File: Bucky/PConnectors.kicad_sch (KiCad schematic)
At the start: 52 parts, among them IC4 LTC4372CMS8#TRPBF, IC5 LTC4372CMS8#TRPBF, IC701 LTC4372CMS8#TRPBF, IC702 LTC4372CMS8#TRPBF, J1 XT60PW-M, J11 XT30AW-M, J12 XT30AW-M, J13 XT30AW-M, J14 XT30AW-M, J17 XT30UPB-F, J18 XT30UPB-F, J2 XT60PW-F, J3 XT30PW-F, J4 XT30PW-F, J5 XT30PW-F, J6 XT30PW-F, J7 XT30UPB-F, J8 XT30UPB-F, Q1 ISC016N04NM7V, Q2 ISC016N04NM7V, Q3 ISC016N04NM7V, Q4 ISC016N04NM7V, Q5 ISC016N04NM7V, Q6 ISC016N04NM7V, Q7 ISC016N04NM7V, Q8 ISC016N04NM7V

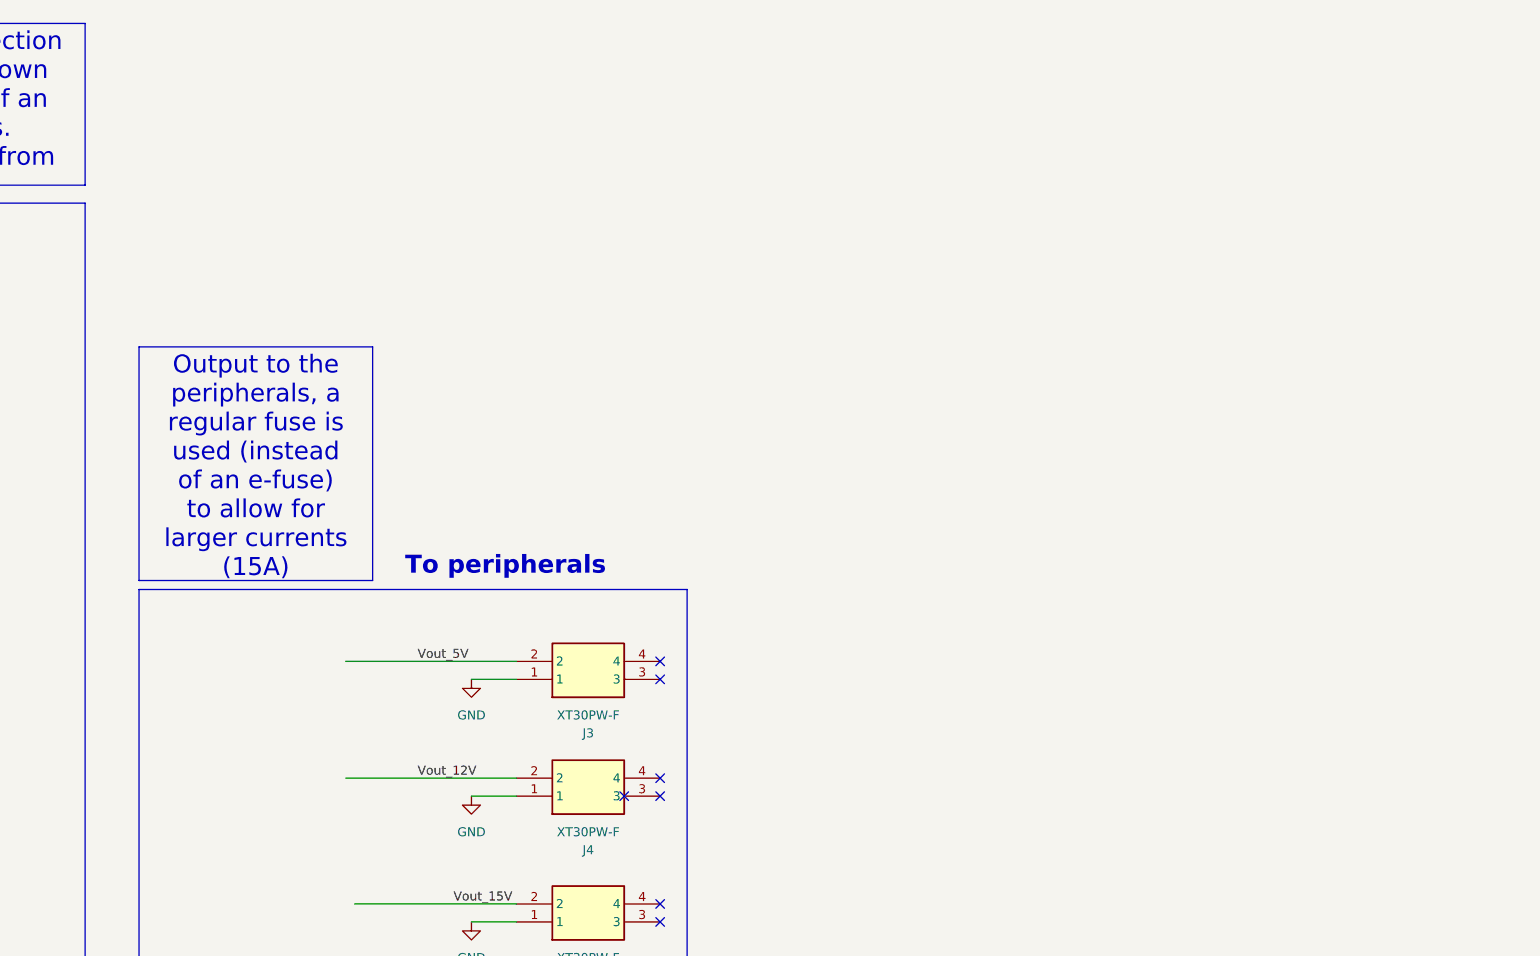
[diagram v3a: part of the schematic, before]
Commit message: created Bucky++ with new template and e-fuses
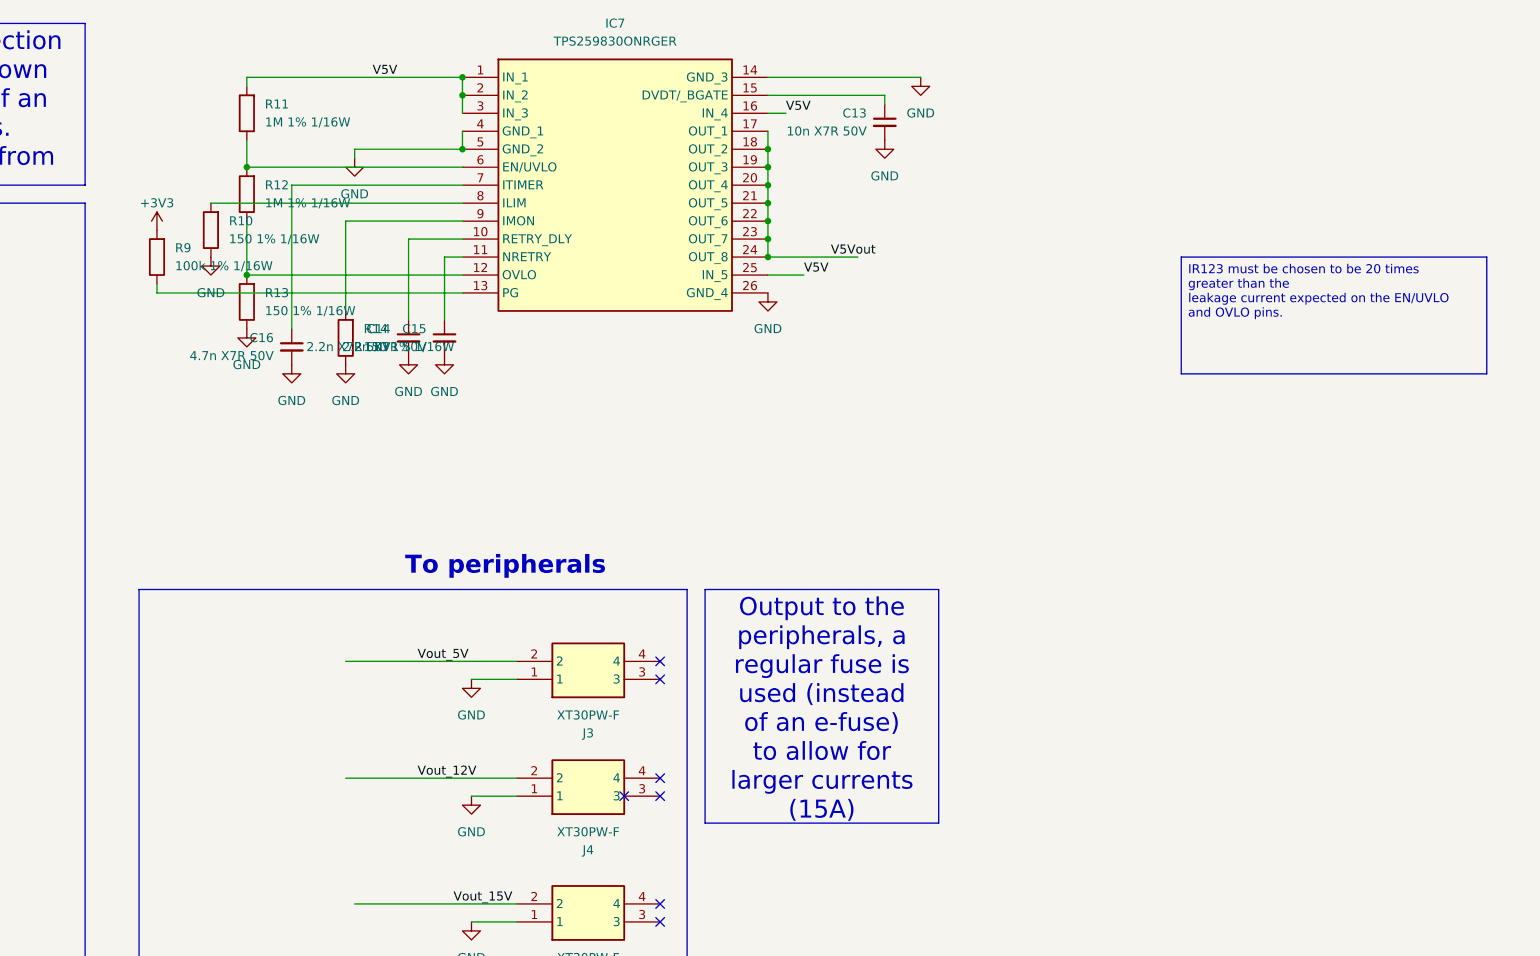
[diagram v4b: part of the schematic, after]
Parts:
- added C13: 10n X7R 50V, 0_capacitor_smd:C_0402_1005_DensityHigh, symbol Device:C_Small
- added C14, C15: 2.2n X7R 50V, 0_capacitor_smd:C_0402_1005_DensityHigh, symbol Device:C_Small
- added C16: 4.7n X7R 50V, 0_capacitor_smd:C_0402_1005_DensityHigh, symbol Device:C_Small
- added IC7: TPS259830ONRGER, TPS259830ONRGER, symbol SamacSys_Parts:TPS259830ONRGER
- added R10, R13, R14: 150 1% 1/16W, 0_resistor_smd:R_0402_1005_DensityHigh, symbol Device:R
- added R11, R12: 1M 1% 1/16W, 0_resistor_smd:R_0402_1005_DensityHigh, symbol Device:R
- added R9: 100k 1% 1/16W, 0_resistor_smd:R_0402_1005_DensityHigh, symbol Device:R
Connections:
- net GND: now also C13.2, C14.2, C15.2, C16.2, IC7.14 (GND_3), IC7.26 (GND_4), IC7.4 (GND_1), IC7.5 (GND_2), R10.1, R13.1, R14.1
- new net: C14.1, IC7.10 (RETRY_DLY)
- new net: C15.1, IC7.11 (NRETRY)
- new net: IC7.12 (OVLO), R12.1, R13.2
- new net: IC7.13 (PG), R9.1
- new net: C13.1, IC7.15 (DVDT/_BGATE)
- new net: IC7.6 (EN/UVLO), R11.1, R12.2
- new net: C16.1, IC7.7 (ITIMER)
- new net: IC7.8 (ILIM), R10.2
- new net: IC7.9 (IMON), R14.2
- new net +3V3: R9.2
- new net V5V: IC7.1 (IN_1), IC7.16 (IN_4), IC7.2 (IN_2), IC7.25 (IN_5), IC7.3 (IN_3), R11.2
- new net V5Vout: IC7.17 (OUT_1), IC7.18 (OUT_2), IC7.19 (OUT_3), IC7.20 (OUT_4), IC7.21 (OUT_5), IC7.22 (OUT_6), IC7.23 (OUT_7), IC7.24 (OUT_8)
